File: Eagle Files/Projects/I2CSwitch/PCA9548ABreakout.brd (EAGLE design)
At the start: 21.6 x 29.2 mm, 16 parts

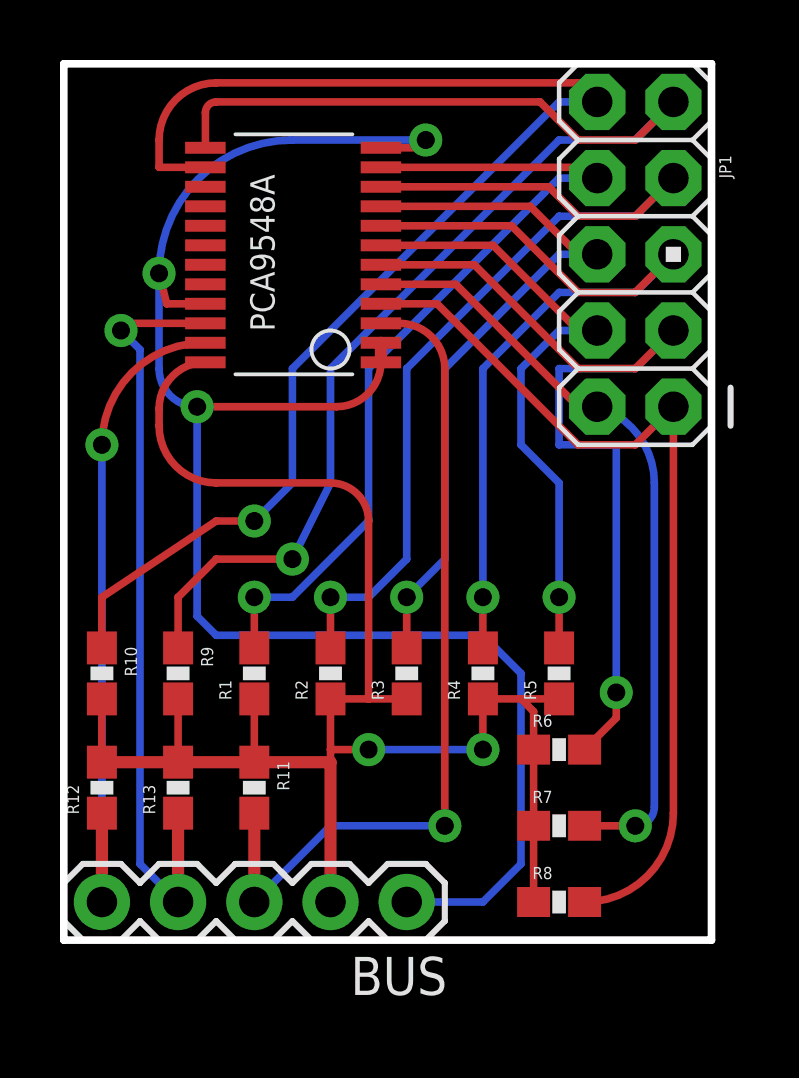
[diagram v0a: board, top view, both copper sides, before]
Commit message: Small adjustments to the I2CSwitch
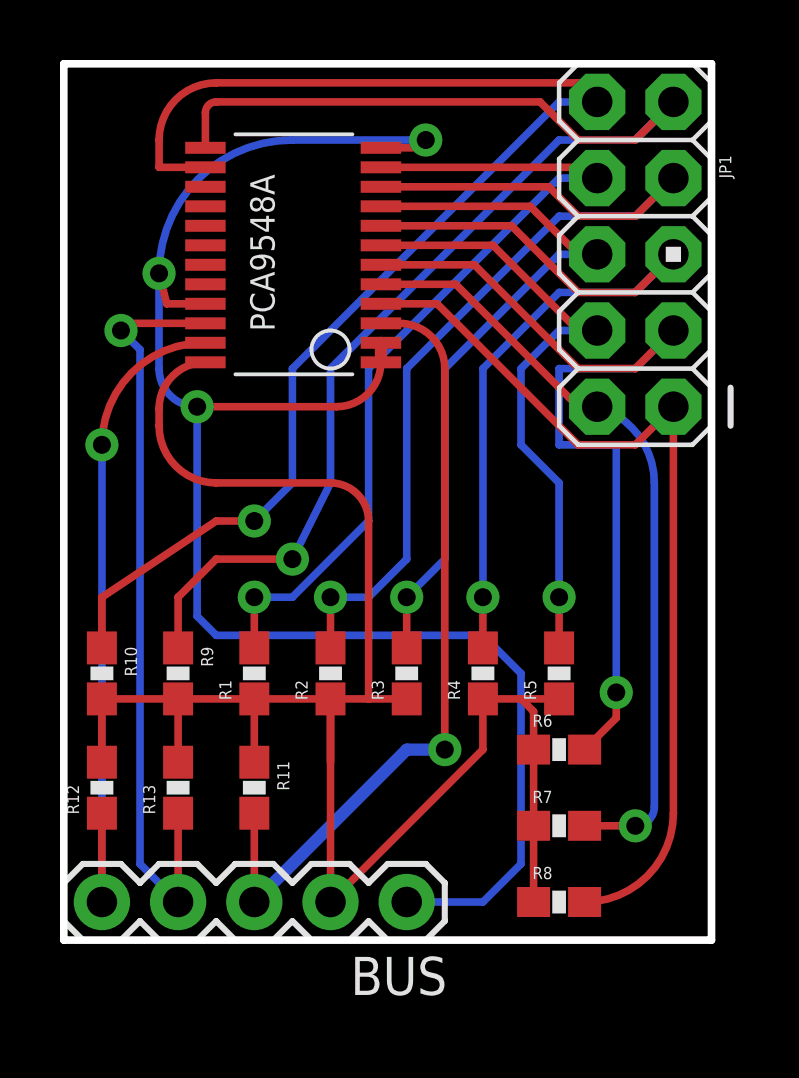
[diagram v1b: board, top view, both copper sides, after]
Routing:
- net VDD: track 56.5 -> 60.7 mm, vias 2 -> 0
- net N$1: track 28.4 -> 26.9 mm
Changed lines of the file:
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@@
 <contactref element="R9" pad="2"/>
 <contactref element="R10" pad="2"/>
-<wire x1="8.89" y1="1.27" x2="8.89" y2="5.93" width="0.4064" layer="1"/>
-<wire x1="8.89" y1="5.93" x2="6.35" y2="5.93" width="0.4064" layer="1"/>
-<wire x1="6.35" y1="5.93" x2="3.81" y2="5.93" width="0.4064" layer="1"/>
-<wire x1="3.81" y1="5.93" x2="1.27" y2="5.93" width="0.4064" layer="1"/>
 <wire x1="15.66" y1="1.27" x2="15.66" y2="3.81" width="0.254" layer="1"/>
 <wire x1="15.66" y1="3.81" x2="15.66" y2="6.35" width="0.254" layer="1"/>
@@
 <wire x1="11.43" y1="8.04" x2="10.16" y2="8.04" width="0.254" layer="1"/>
 <wire x1="10.16" y1="8.04" x2="8.89" y2="8.04" width="0.254" layer="1"/>
-<wire x1="8.89" y1="8.04" x2="8.89" y2="6.35" width="0.254" layer="1"/>
-<wire x1="8.89" y1="6.35" x2="8.89" y2="5.93" width="0.254" layer="1"/>
+<wire x1="8.89" y1="8.04" x2="8.89" y2="5.93" width="0.254" layer="1"/>
 <wire x1="6.35" y1="5.93" x2="6.35" y2="8.04" width="0.254" layer="1"/>
 <wire x1="3.81" y1="5.93" x2="3.81" y2="8.04" width="0.254" layer="1"/>
@@
 <wire x1="10.16" y1="13.97" x2="10.16" y2="8.04" width="0.254" layer="1"/>
 <wire x1="13.97" y1="8.04" x2="13.97" y2="6.35" width="0.254" layer="1"/>
-<via x="13.97" y="6.35" extent="1-16" drill="0.6"/>
-<wire x1="13.97" y1="6.35" x2="10.16" y2="6.35" width="0.254" layer="16"/>
-<via x="10.16" y="6.35" extent="1-16" drill="0.6"/>
-<wire x1="10.16" y1="6.35" x2="8.89" y2="6.35" width="0.254" layer="1"/>
+<wire x1="13.97" y1="6.35" x2="8.89" y2="1.27" width="0.254" layer="1"/>
+<wire x1="8.89" y1="8.04" x2="8.89" y2="1.27" width="0.254" layer="1"/>
+<wire x1="8.89" y1="8.04" x2="6.35" y2="8.04" width="0.254" layer="1"/>
+<wire x1="6.35" y1="8.04" x2="3.81" y2="8.04" width="0.254" layer="1"/>
+<wire x1="3.81" y1="8.04" x2="1.27" y2="8.04" width="0.254" layer="1"/>
 </signal>
 <signal name="GND">
@@
 <contactref element="R11" pad="2"/>
 <contactref element="BUS" pad="3"/>
-<wire x1="6.35" y1="4.23" x2="6.35" y2="1.27" width="0.4064" layer="1"/>
 <wire x1="10.57" y1="20.56" x2="11.19" y2="20.56" width="0.254" layer="1"/>
 <wire x1="11.19" y1="20.56" x2="12.7" y2="19.05" width="0.254" layer="1" curve="-90"/>
-<wire x1="12.7" y1="19.05" x2="12.7" y2="3.81" width="0.254" layer="1"/>
-<via x="12.7" y="3.81" extent="1-16" drill="0.6"/>
-<wire x1="12.7" y1="3.81" x2="8.89" y2="3.81" width="0.254" layer="16"/>
-<wire x1="8.89" y1="3.81" x2="6.35" y2="1.27" width="0.254" layer="16"/>
+<wire x1="12.7" y1="19.05" x2="12.7" y2="6.35" width="0.254" layer="1"/>
+<via x="12.7" y="6.35" extent="1-16" drill="0.6"/>
+<wire x1="12.7" y1="6.35" x2="11.43" y2="6.35" width="0.4064" layer="16"/>
+<wire x1="11.43" y1="6.35" x2="6.35" y2="1.27" width="0.4064" layer="16"/>
+<wire x1="6.35" y1="1.27" x2="6.35" y2="4.23" width="0.254" layer="1"/>
 </signal>
 <signal name="SCL">
@@
 <contactref element="PCA9548A" pad="SCL"/>
 <contactref element="R13" pad="1"/>
-<wire x1="3.81" y1="4.23" x2="3.81" y2="1.27" width="0.4064" layer="1"/>
 <wire x1="4.72" y1="20.56" x2="2.145" y2="20.56" width="0.254" layer="1"/>
 <wire x1="2.145" y1="20.56" x2="1.905" y2="20.32" width="0.254" layer="1"/>
@@
 <wire x1="2.54" y1="19.685" x2="2.54" y2="2.54" width="0.254" layer="16"/>
 <wire x1="2.54" y1="2.54" x2="3.81" y2="1.27" width="0.254" layer="16"/>
+<wire x1="3.81" y1="4.23" x2="3.81" y2="1.27" width="0.254" layer="1"/>
 </signal>
 <signal name="SDA">
@@
 <contactref element="R12" pad="1"/>
 <contactref element="PCA9548A" pad="SDA"/>
-<wire x1="1.27" y1="4.23" x2="1.27" y2="1.27" width="0.4064" layer="1"/>
 <wire x1="4.72" y1="19.91" x2="4.67" y2="19.91" width="0.254" layer="1"/>
 <wire x1="4.67" y1="19.91" x2="1.27" y2="16.51" width="0.254" layer="1" curve="90"/>
 <via x="1.27" y="16.51" extent="1-16" drill="0.6"/>
 <wire x1="1.27" y1="16.51" x2="1.27" y2="1.27" width="0.254" layer="16"/>
+<wire x1="1.27" y1="1.27" x2="1.27" y2="4.23" width="0.254" layer="1"/>
 </signal>
 <signal name="N$10">
